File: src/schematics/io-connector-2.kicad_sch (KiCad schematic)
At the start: 1 part, among them J13 DDR4_SODIMM_Board

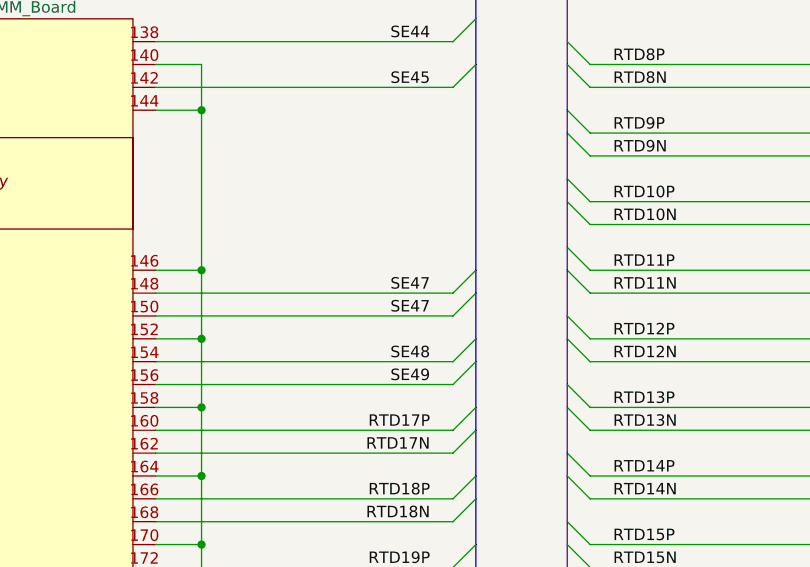
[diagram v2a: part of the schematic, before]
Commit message: Start routing the io diff pairs
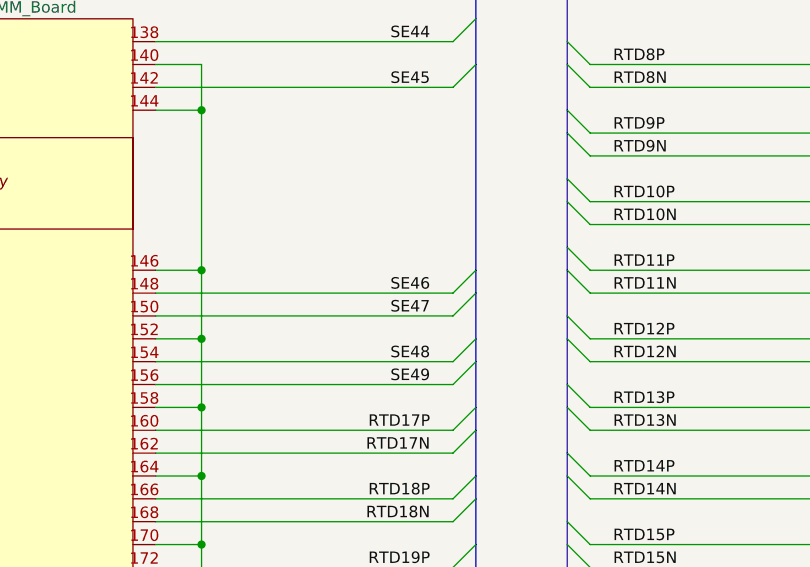
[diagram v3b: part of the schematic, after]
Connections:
- net SE47: no longer J13.148
- new net SE46: J13.148
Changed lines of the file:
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@@
 		)
 	)
-	(label "SE47"
+	(label "SE46"
 		(at 140.97 78.74 180)
 		(effects

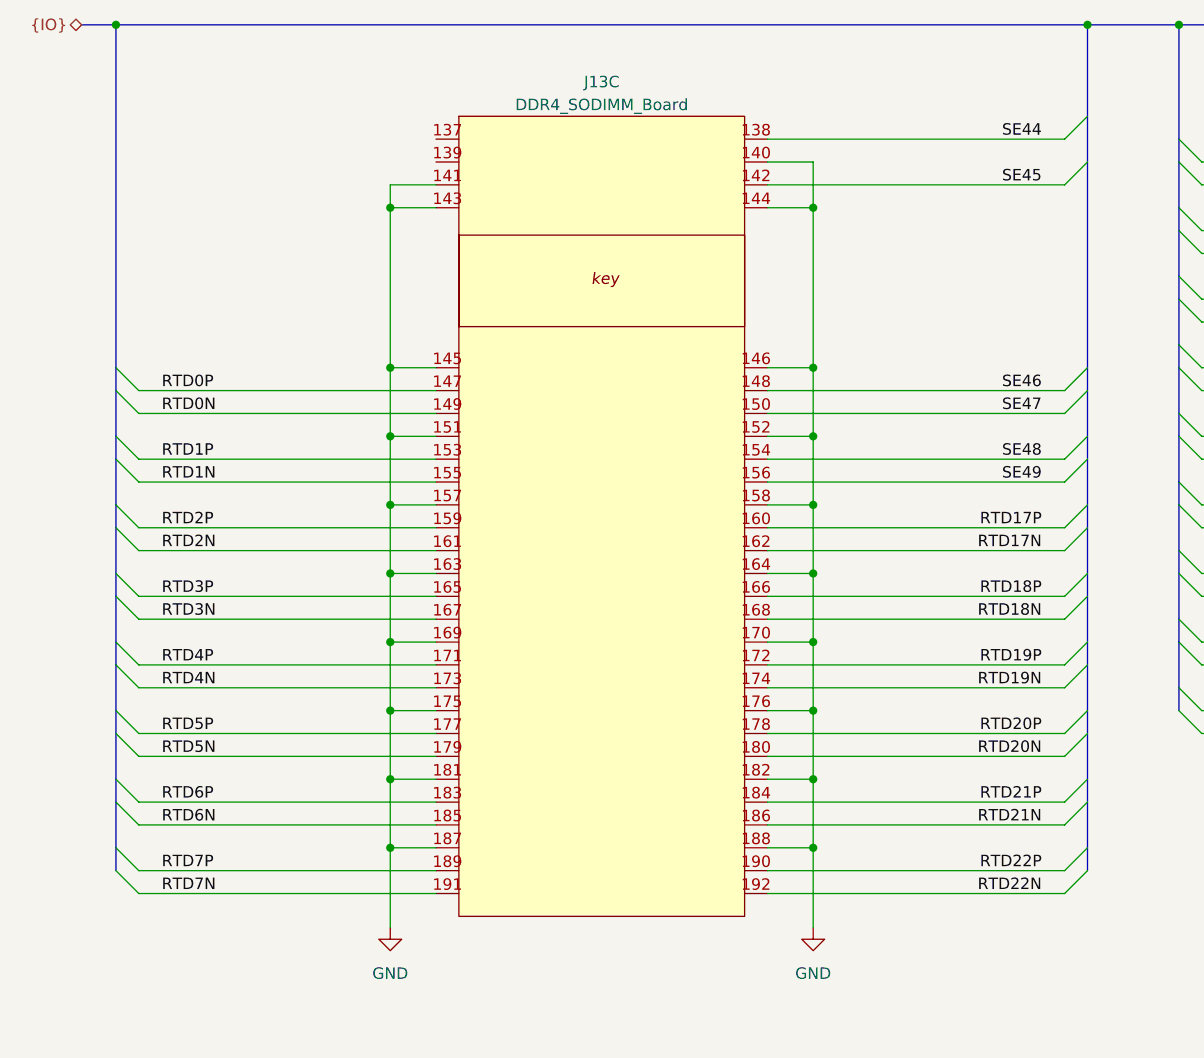
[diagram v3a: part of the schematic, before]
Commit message: Continue routing the io connector
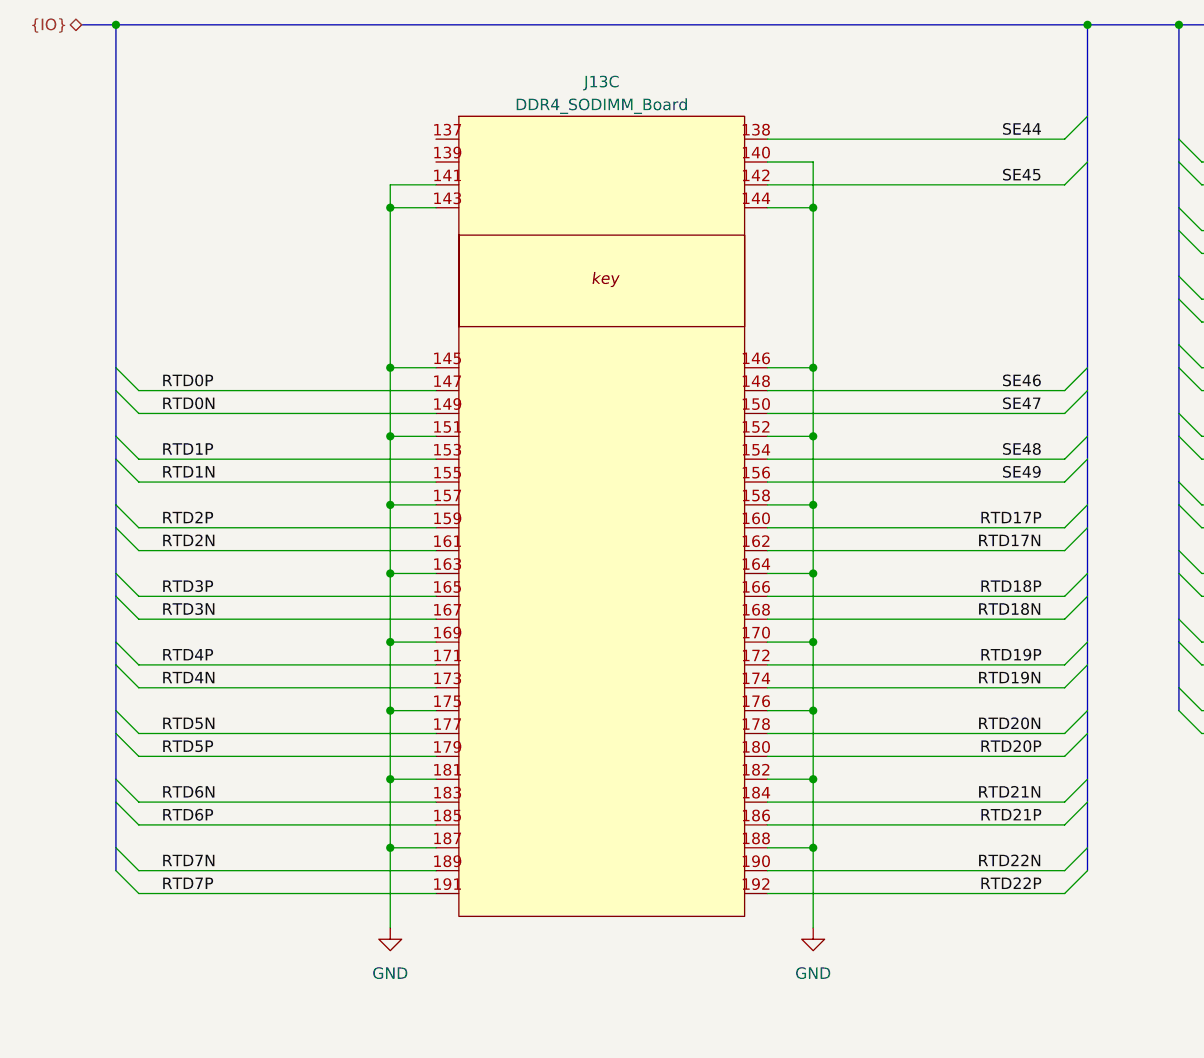
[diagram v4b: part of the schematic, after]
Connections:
- net RTD20N: now also J13.178; no longer J13.180
- net RTD20P: now also J13.180; no longer J13.178
- net RTD21N: now also J13.184; no longer J13.186
- net RTD21P: now also J13.186; no longer J13.184
- net RTD22N: now also J13.190; no longer J13.192
- net RTD22P: now also J13.192; no longer J13.190
- net RTD5N: now also J13.177; no longer J13.179
- net RTD5P: now also J13.179; no longer J13.177
- net RTD6N: now also J13.183; no longer J13.185
- net RTD6P: now also J13.185; no longer J13.183
- net RTD7N: now also J13.189; no longer J13.191
- net RTD7P: now also J13.191; no longer J13.189
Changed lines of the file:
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@@
-	(wire
-		(pts
-			(xy 115.57 53.34) (xy 110.49 53.34)
-		)
-		(stroke
-			(width 0)
-			(type default)
-		)
-	)
 	(wire
 		(pts
@@
 		(pts
 			(xy 185.42 111.76) (xy 190.5 111.76)
+		)
+		(stroke
+			(width 0)
+			(type default)
+		)
+	)
+	(wire
+		(pts
+			(xy 110.49 53.34) (xy 115.57 53.34)
 		)
 		(stroke
@@
 	)
 	(label "RTD7N"
-		(at 43.18 134.62 0)
+		(at 43.18 132.08 0)
 		(effects
 			(font
@@
 	)
 	(label "RTD20P"
-		(at 140.97 116.84 180)
+		(at 140.97 119.38 180)
 		(effects
 			(font
@@
 	)
 	(label "RTD21N"
-		(at 140.97 127 180)
+		(at 140.97 124.46 180)
 		(effects
 			(font
@@
 	)
 	(label "RTD6P"
-		(at 43.18 124.46 0)
+		(at 43.18 127 0)
 		(effects
 			(font
@@
 	)
 	(label "RTD5N"
-		(at 43.18 119.38 0)
+		(at 43.18 116.84 0)
 		(effects
 			(font
@@
 	)
 	(label "RTD22N"
-		(at 140.97 134.62 180)
+		(at 140.97 132.08 180)
 		(effects
 			(font
@@
 	)
 	(label "RTD20N"
-		(at 140.97 119.38 180)
+		(at 140.97 116.84 180)
 		(effects
 			(font
@@
 	)
 	(label "RTD6N"
-		(at 43.18 127 0)
+		(at 43.18 124.46 0)
 		(effects
 			(font
@@
 	)
 	(label "RTD21P"
-		(at 140.97 124.46 180)
+		(at 140.97 127 180)
 		(effects
 			(font
@@
 	)
 	(label "RTD7P"
-		(at 43.18 132.08 0)
+		(at 43.18 134.62 0)
 		(effects
 			(font
@@
 	)
 	(label "RTD5P"
-		(at 43.18 116.84 0)
+		(at 43.18 119.38 0)
 		(effects
 			(font
@@
 	)
 	(label "RTD22P"
-		(at 140.97 132.08 180)
+		(at 140.97 134.62 180)
 		(effects
 			(font
@@
 		(on_board yes)
 		(dnp no)
-		(fields_autoplaced yes)
 		(property "Reference" "J13"
 			(at 92.075 44.45 0)

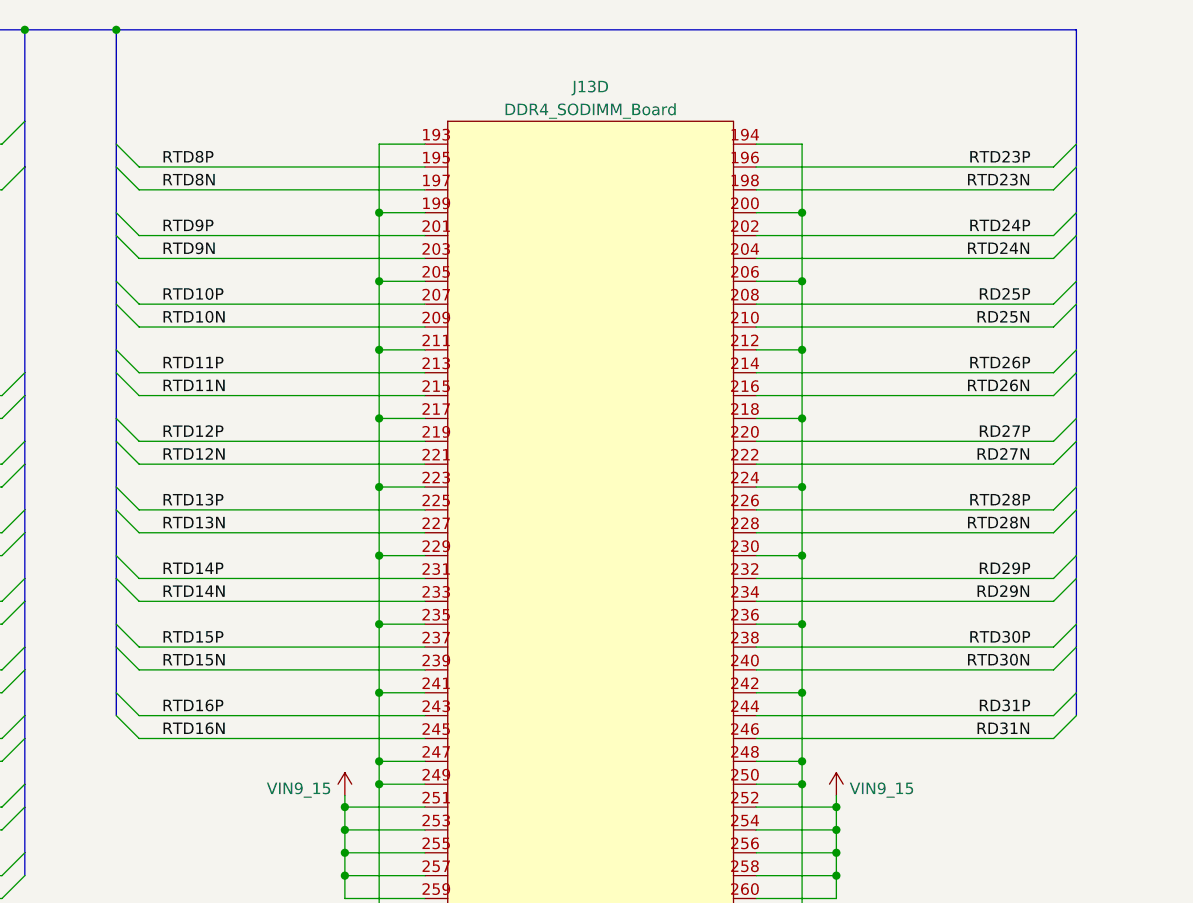
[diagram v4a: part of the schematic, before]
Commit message: Finish routing the io connector
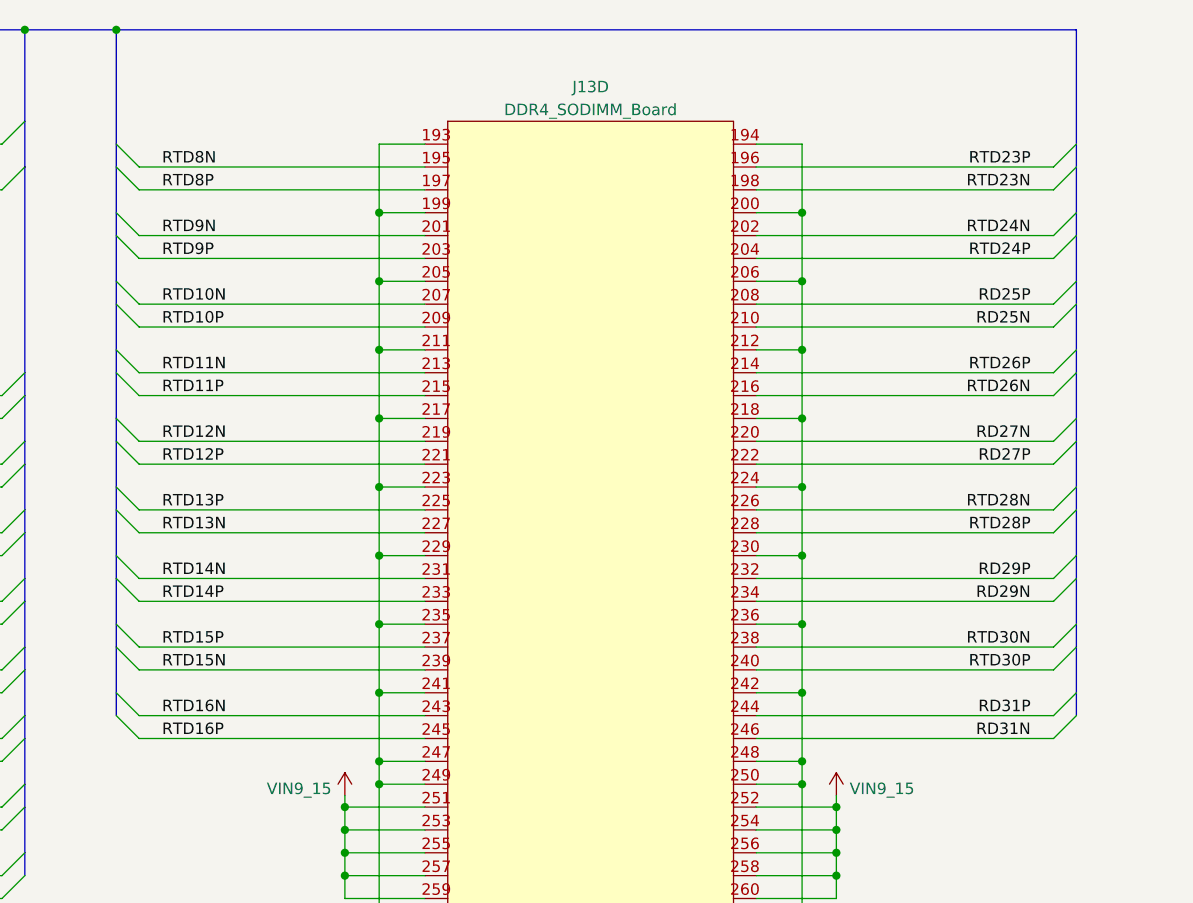
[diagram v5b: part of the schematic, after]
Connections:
- net RD27N: now also J13.220; no longer J13.222
- net RD27P: now also J13.222; no longer J13.220
- net RTD10N: now also J13.207; no longer J13.209
- net RTD10P: now also J13.209; no longer J13.207
- net RTD11N: now also J13.213; no longer J13.215
- net RTD11P: now also J13.215; no longer J13.213
- net RTD12N: now also J13.219; no longer J13.221
- net RTD12P: now also J13.221; no longer J13.219
- net RTD14N: now also J13.231; no longer J13.233
- net RTD14P: now also J13.233; no longer J13.231
- net RTD16N: now also J13.243; no longer J13.245
- net RTD16P: now also J13.245; no longer J13.243
- net RTD24N: now also J13.202; no longer J13.204
- net RTD24P: now also J13.204; no longer J13.202
- net RTD28N: now also J13.226; no longer J13.228
- net RTD28P: now also J13.228; no longer J13.226
- net RTD30N: now also J13.238; no longer J13.240
- net RTD30P: now also J13.240; no longer J13.238
- net RTD8N: now also J13.195; no longer J13.197
- net RTD8P: now also J13.197; no longer J13.195
- net RTD9N: now also J13.201; no longer J13.203
- net RTD9P: now also J13.203; no longer J13.201
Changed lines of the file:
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@@
 	)
 	(label "RTD12N"
-		(at 161.29 86.36 0)
+		(at 161.29 83.82 0)
 		(effects
 			(font
@@
 	)
 	(label "RTD8N"
-		(at 161.29 55.88 0)
+		(at 161.29 53.34 0)
 		(effects
 			(font
@@
 	)
 	(label "RTD14N"
-		(at 161.29 101.6 0)
+		(at 161.29 99.06 0)
 		(effects
 			(font
@@
 	)
 	(label "RD27P"
-		(at 257.81 83.82 180)
+		(at 257.81 86.36 180)
 		(effects
 			(font
@@
 	)
 	(label "RTD12P"
-		(at 161.29 83.82 0)
+		(at 161.29 86.36 0)
 		(effects
 			(font
@@
 	)
 	(label "RTD10P"
-		(at 161.29 68.58 0)
+		(at 161.29 71.12 0)
 		(effects
 			(font
@@
 	)
 	(label "RTD8P"
-		(at 161.29 53.34 0)
+		(at 161.29 55.88 0)
 		(effects
 			(font
@@
 	)
 	(label "RTD9N"
-		(at 161.29 63.5 0)
+		(at 161.29 60.96 0)
 		(effects
 			(font
@@
 	)
 	(label "RTD30N"
-		(at 257.81 109.22 180)
+		(at 257.81 106.68 180)
 		(effects
 			(font
@@
 	)
 	(label "RTD24P"
-		(at 257.81 60.96 180)
+		(at 257.81 63.5 180)
 		(effects
 			(font
@@
 	)
 	(label "RTD28P"
-		(at 257.81 91.44 180)
+		(at 257.81 93.98 180)
 		(effects
 			(font
@@
 	)
 	(label "RTD9P"
-		(at 161.29 60.96 0)
+		(at 161.29 63.5 0)
 		(effects
 			(font
@@
 	)
 	(label "RTD11P"
-		(at 161.29 76.2 0)
+		(at 161.29 78.74 0)
 		(effects
 			(font
@@
 	)
 	(label "RD27N"
-		(at 257.81 86.36 180)
+		(at 257.81 83.82 180)
 		(effects
 			(font
@@
 	)
 	(label "RTD30P"
-		(at 257.81 106.68 180)
+		(at 257.81 109.22 180)
 		(effects
 			(font
@@
 	)
 	(label "RTD24N"
-		(at 257.81 63.5 180)
+		(at 257.81 60.96 180)
 		(effects
 			(font
@@
 	)
 	(label "RTD14P"
-		(at 161.29 99.06 0)
+		(at 161.29 101.6 0)
 		(effects
 			(font
@@
 	)
 	(label "RTD11N"
-		(at 161.29 78.74 0)
+		(at 161.29 76.2 0)
 		(effects
 			(font
@@
 	)
 	(label "RTD10N"
-		(at 161.29 71.12 0)
+		(at 161.29 68.58 0)
 		(effects
 			(font
@@
 	)
 	(label "RTD16P"
-		(at 161.29 114.3 0)
+		(at 161.29 116.84 0)
 		(effects
 			(font
@@
 	)
 	(label "RTD16N"
-		(at 161.29 116.84 0)
+		(at 161.29 114.3 0)
 		(effects
 			(font
@@
 	)
 	(label "RTD28N"
-		(at 257.81 93.98 180)
-		(effects
-			(font
+		(at 257.81 91.44 180)
+		(effects
+			(font

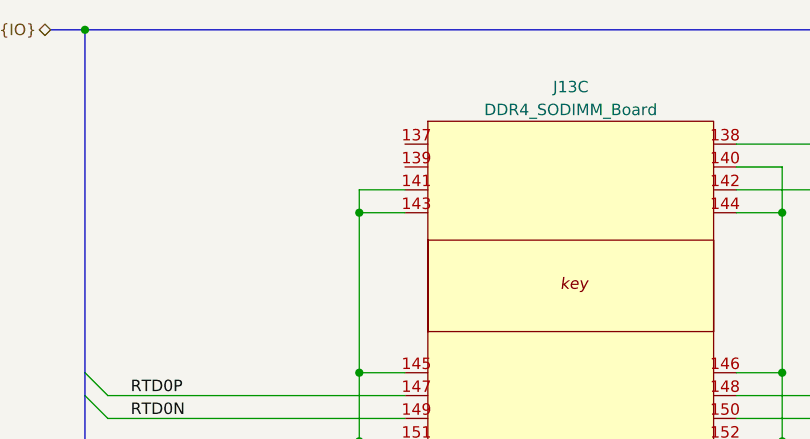
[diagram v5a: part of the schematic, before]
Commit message: Fix ERC after routing completion
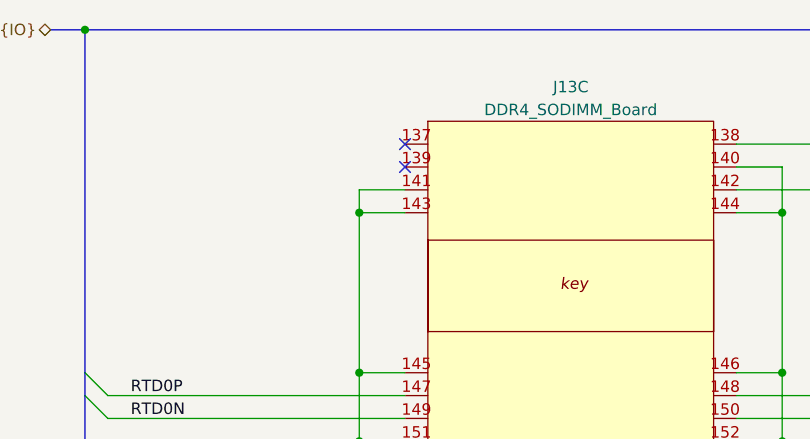
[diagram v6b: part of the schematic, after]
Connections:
- no-connect marks 0 -> 2
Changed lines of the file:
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@@
 		(color 0 0 0 0)
+	)
+	(no_connect
+		(at 73.66 50.8)
+	)
+	(no_connect
+		(at 73.66 53.34)
 	)
 	(bus_entry
